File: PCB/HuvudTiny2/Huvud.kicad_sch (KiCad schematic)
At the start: 104 parts, among them J1 Vin, J12 USB_Micro-B, J2 DBG, J3 THERM, J4 FAN0, J5 FAN1, J6 Heater, J7 Endstop, J9 STEPPER, Q1 AO3400A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

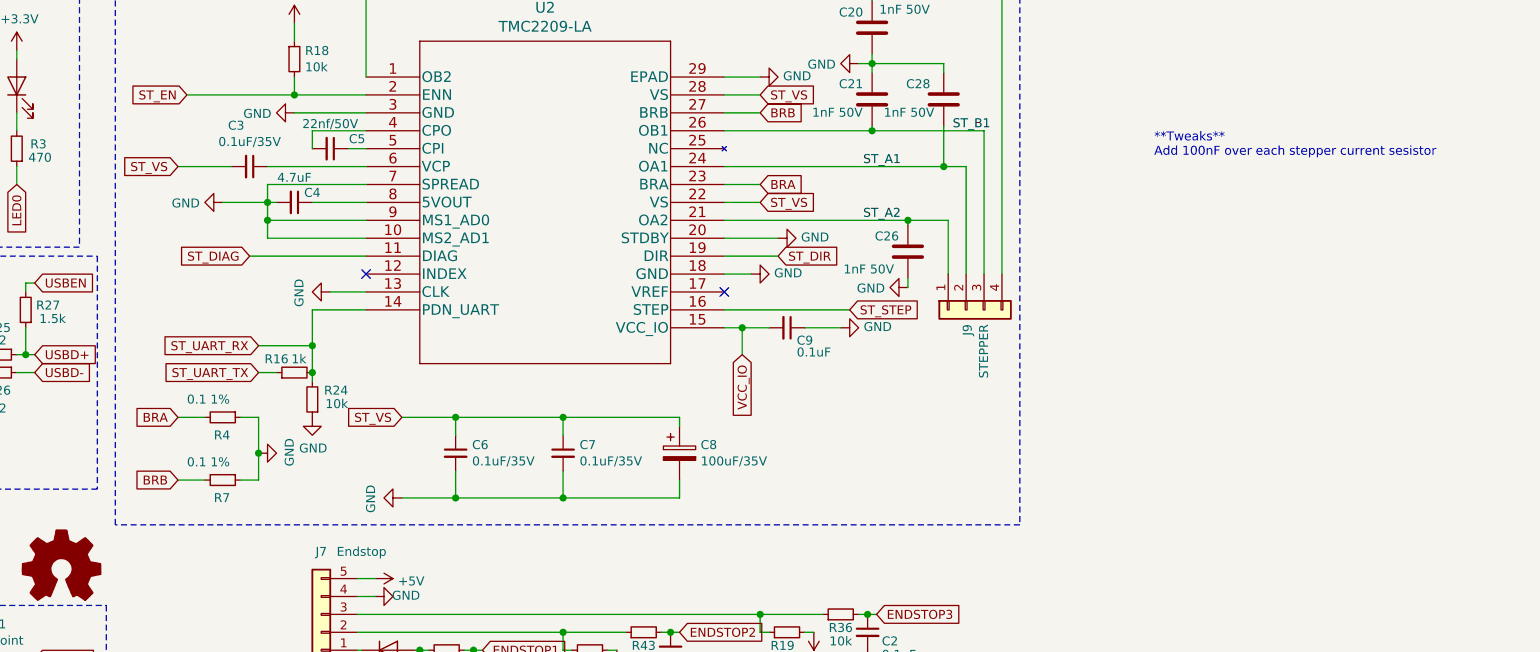
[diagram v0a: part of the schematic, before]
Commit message: Add caps across current sense resistors.
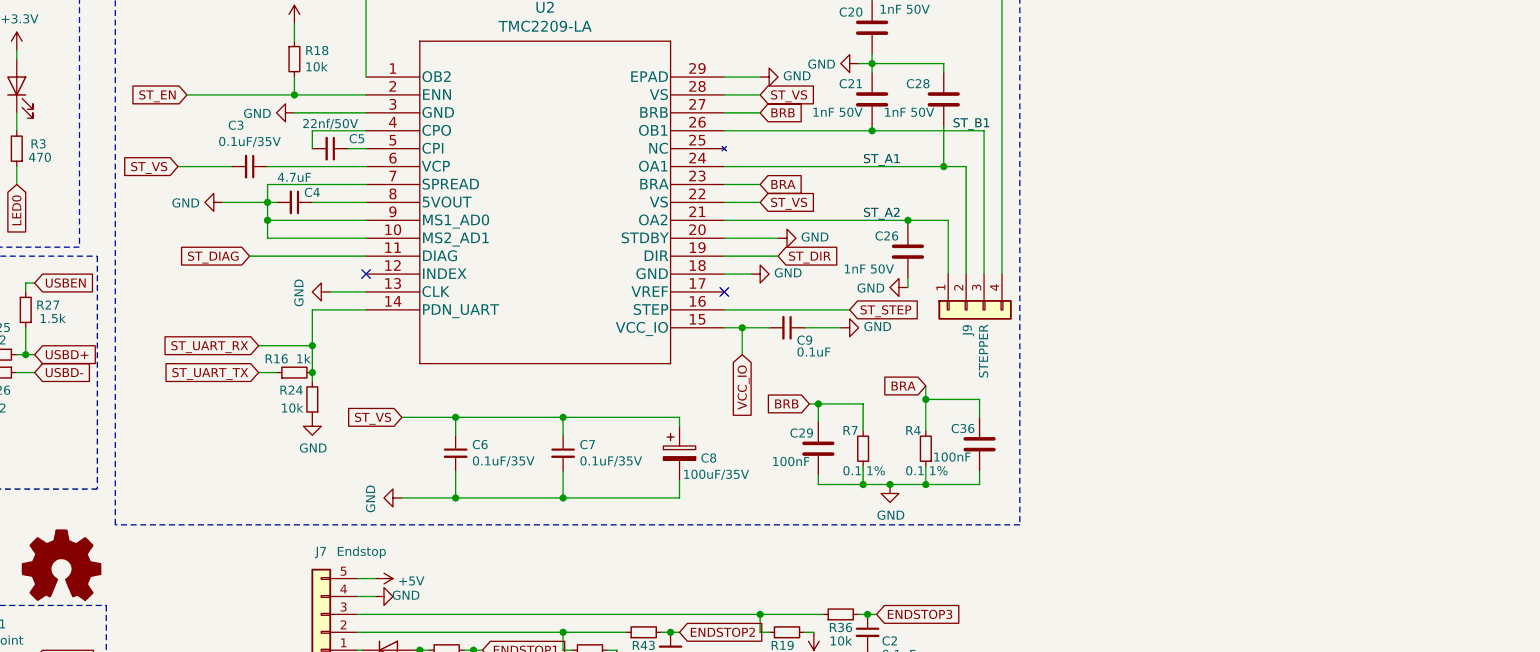
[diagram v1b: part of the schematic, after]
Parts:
- added C29, C36: 100nF, Capacitor_SMD:C_0402_1005Metric, symbol Device:C
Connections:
- net BRA: now also C36.1
- net BRB: now also C29.1
- net GND: now also C29.2, C36.2
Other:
- note removed: "**Tweaks** Add 100nF over each stepper current sesistor"
- moved on the sheet: R4, R7

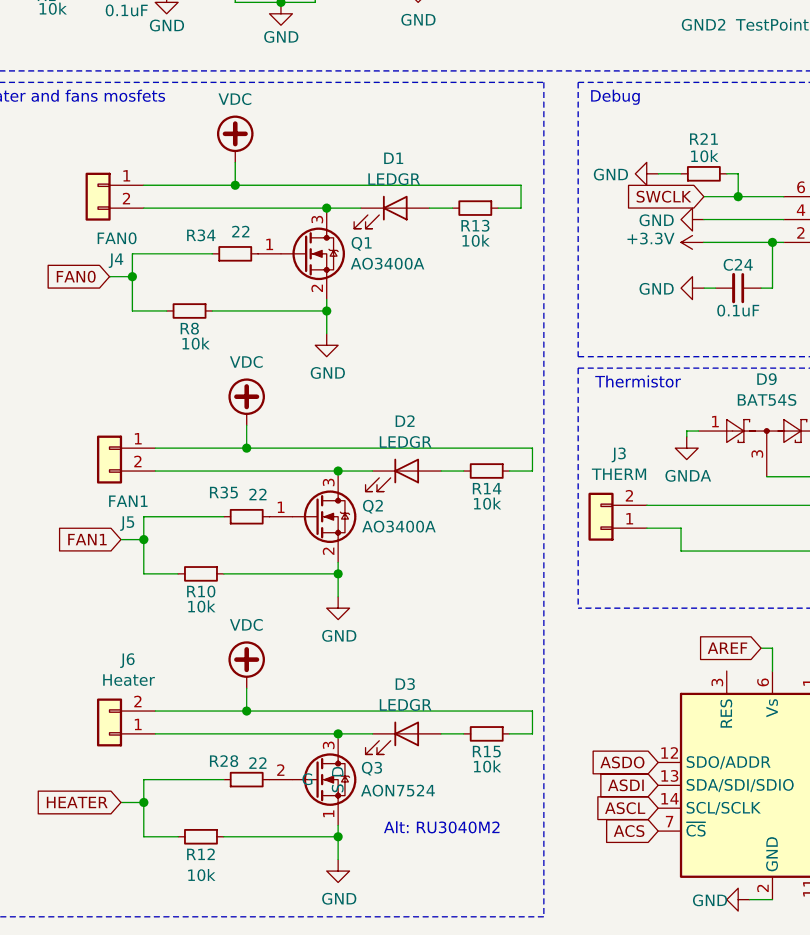
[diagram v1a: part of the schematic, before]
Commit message: Small tweaks to footprints.
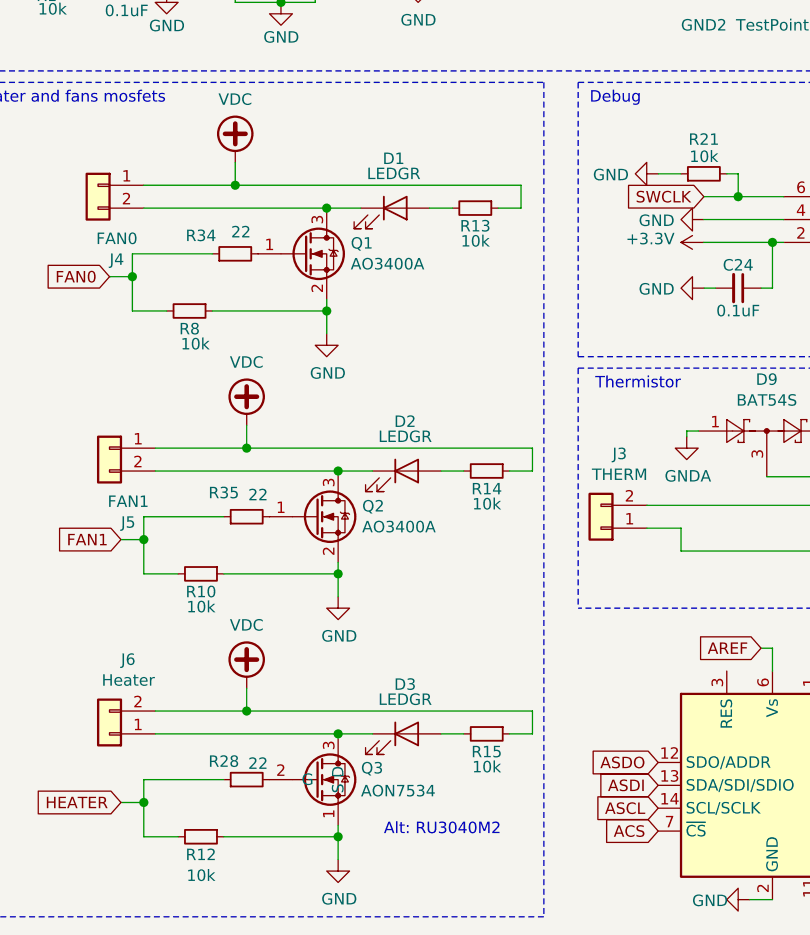
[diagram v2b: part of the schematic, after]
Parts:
- C22: footprint Capacitor_SMD:C_1210_3225Metric -> Capacitor_SMD:C_1206_3216Metric
- Q3: value AON7524 -> AON7534
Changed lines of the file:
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@@
     (property "Reference" "C22" (id 0) (at 251.46 151.765 0))
     (property "Value" "10uF/35V" (id 1) (at 255.905 149.225 90))
-    (property "Footprint" "Capacitor_SMD:C_1210_3225Metric" (id 2) (at 253.365 149.86 0)
+    (property "Footprint" "Capacitor_SMD:C_1206_3216Metric" (id 2) (at 253.365 149.86 0)
       (effects (font (size 1.27 1.27)) hide)
     )
@@
     (in_bom yes) (on_board yes)
     (property "Reference" "D1" (id 0) (at 60.7822 111.3536 0))
-    (property "Value" "LEDGR" (id 1) (at 60.7822 113.665 0))
+    (property "Value" "LEDGR" (id 1) (at 60.7822 113.03 0))
     (property "Footprint" "LED_SMD:LED_0402_1005Metric" (id 2) (at 60.96 116.84 0)
       (effects (font (size 1.27 1.27)) hide)
@@
     (in_bom yes) (on_board yes)
     (property "Reference" "D2" (id 0) (at 62.0522 140.5636 0))
-    (property "Value" "LEDGR" (id 1) (at 62.0522 142.875 0))
+    (property "Value" "LEDGR" (id 1) (at 62.0522 142.24 0))
     (property "Footprint" "LED_SMD:LED_0402_1005Metric" (id 2) (at 62.23 146.05 0)
       (effects (font (size 1.27 1.27)) hide)
@@
     (in_bom yes) (on_board yes)
     (property "Reference" "D3" (id 0) (at 62.0522 169.7736 0))
-    (property "Value" "LEDGR" (id 1) (at 62.0522 172.085 0))
+    (property "Value" "LEDGR" (id 1) (at 62.0522 171.45 0))
     (property "Footprint" "LED_SMD:LED_0402_1005Metric" (id 2) (at 62.23 175.26 0)
       (effects (font (size 1.27 1.27)) hide)
@@
       (effects (font (size 1.27 1.27)) (justify left))
     )
-    (property "Value" "AON7524" (id 1) (at 57.15 181.61 0)
+    (property "Value" "AON7534" (id 1) (at 57.15 181.61 0)
       (effects (font (size 1.27 1.27)) (justify left))
     )
@@
     )
     (path "/00000000-0000-0000-0000-00005f85ea85"
-      (reference "C22") (unit 1) (value "10uF/35V") (footprint "Capacitor_SMD:C_1210_3225Metric")
+      (reference "C22") (unit 1) (value "10uF/35V") (footprint "Capacitor_SMD:C_1206_3216Metric")
     )
     (path "/00000000-0000-0000-0000-00005f59faa3"
@@
     )
     (path "/00000000-0000-0000-0000-00005f1a1e38"
-      (reference "Q3") (unit 1) (value "AON7524") (footprint "Huvud:DFN-8-1EP_3x3mm_P0.65mm_EP1.7x2.05mm")
+      (reference "Q3") (unit 1) (value "AON7534") (footprint "Huvud:DFN-8-1EP_3x3mm_P0.65mm_EP1.7x2.05mm")
     )
     (path "/00000000-0000-0000-0000-00005f443551"

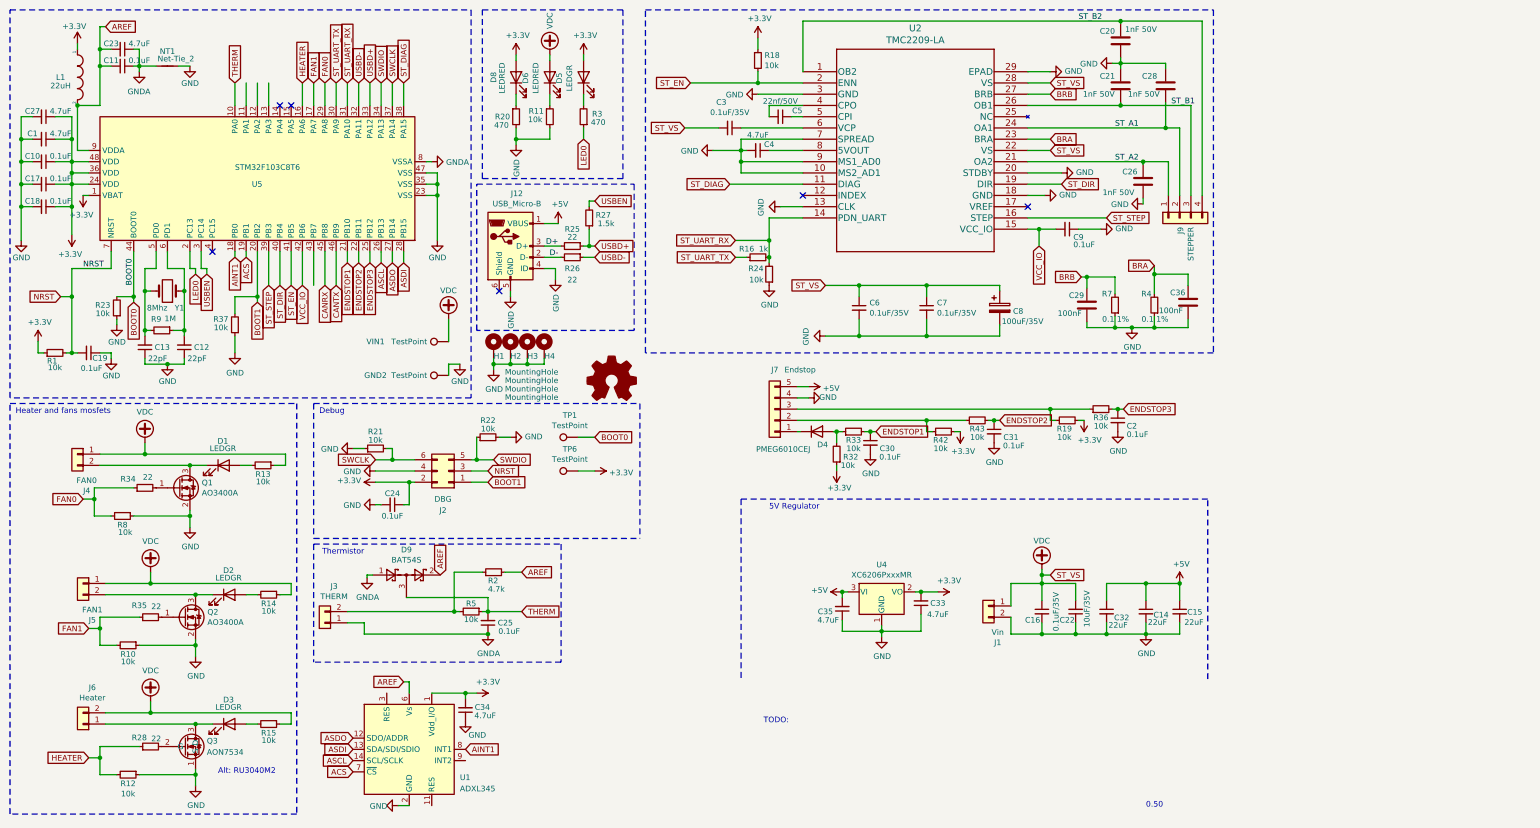
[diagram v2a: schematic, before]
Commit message: Replaced MCU with SAMD21
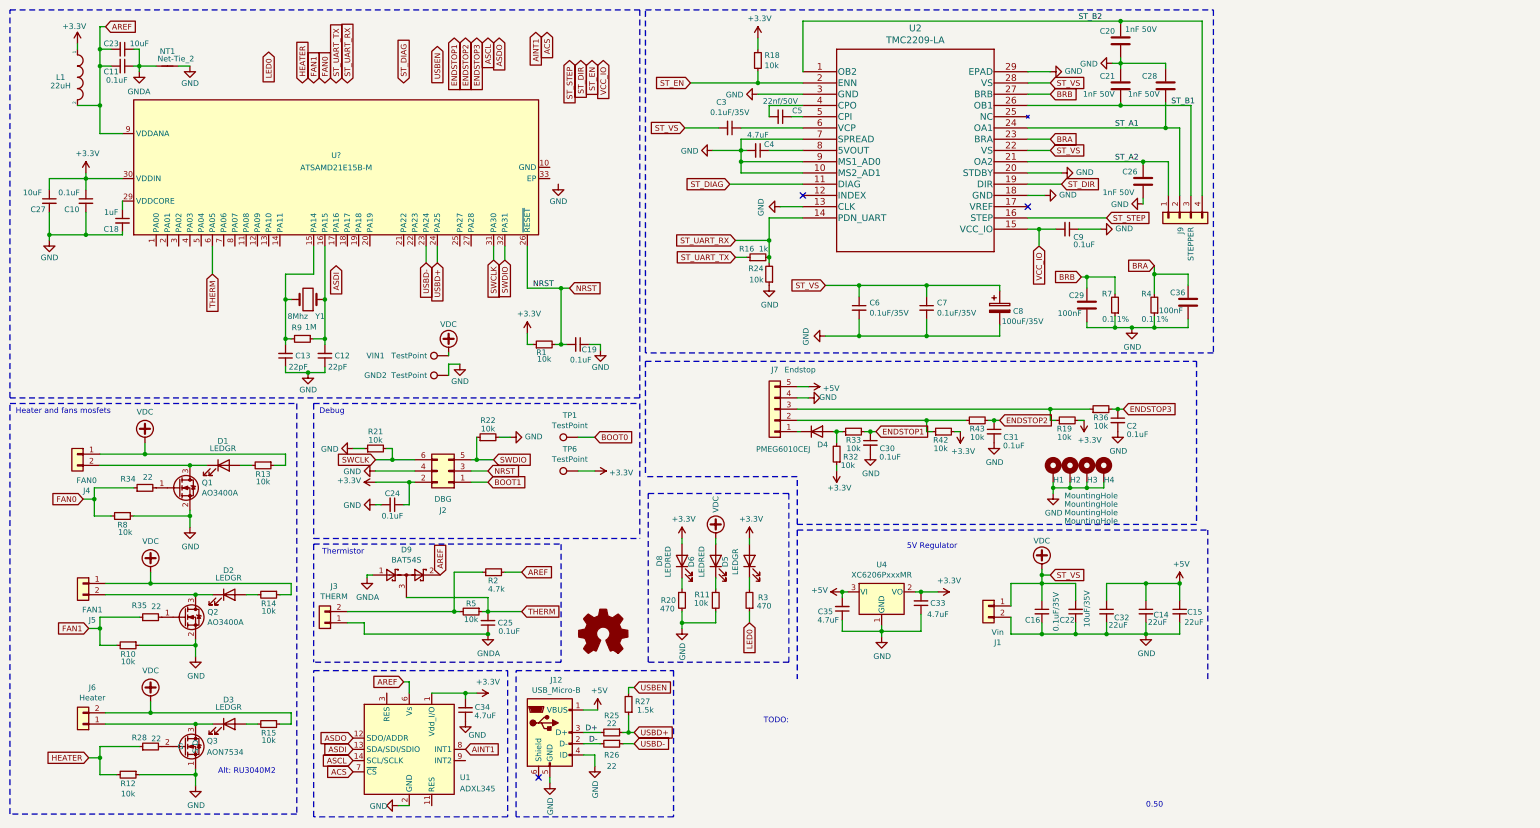
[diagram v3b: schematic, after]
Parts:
- removed C1: 4.7uF, Capacitor_SMD:C_0402_1005Metric, symbol Device:C_Small
- removed C17: 0.1uF, Capacitor_SMD:C_0402_1005Metric, symbol Device:C_Small
- removed R23, R37: 10k, Resistor_SMD:R_0402_1005Metric, symbol Device:R_Small
- removed U5: STM32F103C8T6, Package_QFP:LQFP-48_7x7mm_P0.5mm, symbol MCU_ST_STM32F1:STM32F103C8Tx
- added U?: ATSAMD21E15B-M, Package_DFN_QFN:QFN-32-1EP_5x5mm_P0.5mm_EP3.6x3.6mm, symbol MCU_Microchip_SAMD:ATSAMD21E15B-M
- C18: value 0.1uF -> 1uF; LCSC C1525 -> C52923
- C23, C27: value 4.7uF -> 10uF; LCSC C23733 -> C15525
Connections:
- net +3V3: now also U?.30 (VDDIN); no longer C18.1
- net AREF: now also U?.9 (VDDANA)
- net NRST: now also U?.26 (~{RESET})
- net SWCLK: now also U?.31 (PA30)
- net SWDIO: now also U?.32 (PA31)
- net THERM: now also U?.6 (PA05)
- net USBD+: now also U?.24 (PA25)
- net USBD-: now also U?.23 (PA24)
- net at C13.2, R9.2, Y1.2: now also U?.15 (PA14)
- net at C12.2, R9.1, Y1.1: now also U?.16 (PA15)
- new net: C18.1, U?.29 (VDDCORE)
- new net: U?.10 (GND), U?.28 (GND)
- no-connect marks 6 -> 3
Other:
- moved on the sheet: C10, C12, C13, C18, C19, C27, D5, D6, D8, H1, H2, H3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

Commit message: Some routing.
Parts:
- removed GND2, TP1, TP6, VIN1: TestPoint, TestPoint:TestPoint_Pad_D1.0mm, symbol Connector:TestPoint
- removed R27: 1.5k, Resistor_SMD:R_0402_1005Metric, symbol Device:R_Small
- removed R9: 1M, Resistor_SMD:R_0402_1005Metric, symbol Device:R_Small
- added R6: 1k, Resistor_SMD:R_0402_1005Metric, symbol Device:R_Small
- gave numbers to parts that had none: 1
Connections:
- net +3V3: now also R6.1
- net ACS: now also U3.19 (PA18)
- net AINT1: now also U3.5 (PA04)
- net ASCL: now also U3.18 (PA17)
- net ASDI: now also U3.17 (PA16)
- net ASDO: now also U3.20 (PA19)
- net ENDSTOP1: now also U3.1 (PA00)
- net ENDSTOP2: now also U3.2 (PA01)
- net ENDSTOP3: now also U3.3 (PA02)
- net FAN0: now also U3.8 (PA07)
- net FAN1: now also U3.11 (PA08)
- net GND: now also U3.10 (GND), U3.28 (GND), U3.33 (EP)
- net HEATER: now also U3.7 (PA06)
- net LED0: now also U3.25 (PA27)
- net ST_DIAG: now also U3.4 (PA03)
- net ST_DIR: now also U3.22 (PA23)
- net ST_EN: now also U3.12 (PA09)
- net ST_STEP: now also U3.21 (PA22)
- net ST_UART_RX: now also U3.14 (PA11)
- net ST_UART_TX: now also U3.13 (PA10)
- net SWCLK: now also R6.2
- net VCC_IO: now also U3.27 (PA28)
- net BOOT1: no longer names the net of J2.1 (Pin_1)
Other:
- moved on the sheet: C12, C13, Y1

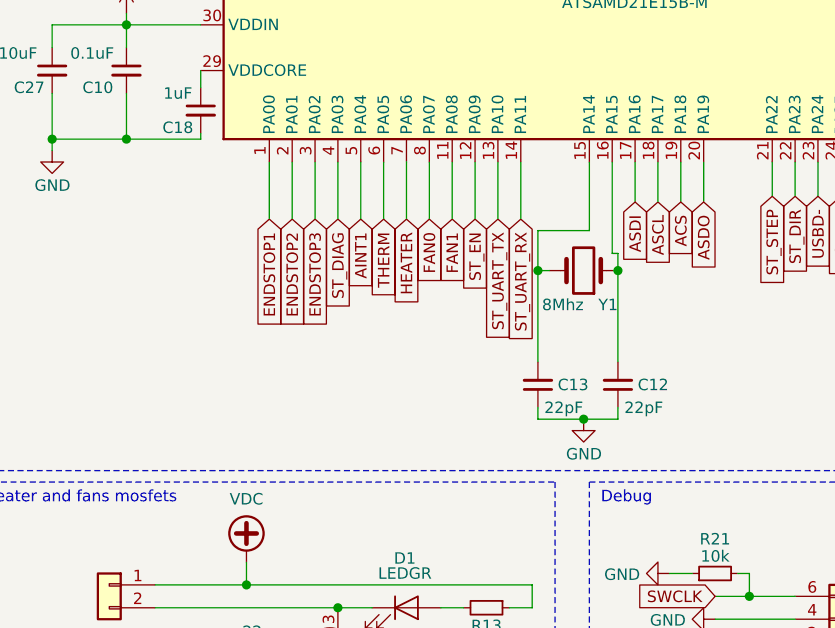
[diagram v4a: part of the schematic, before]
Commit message: Routed with 32k crystal.
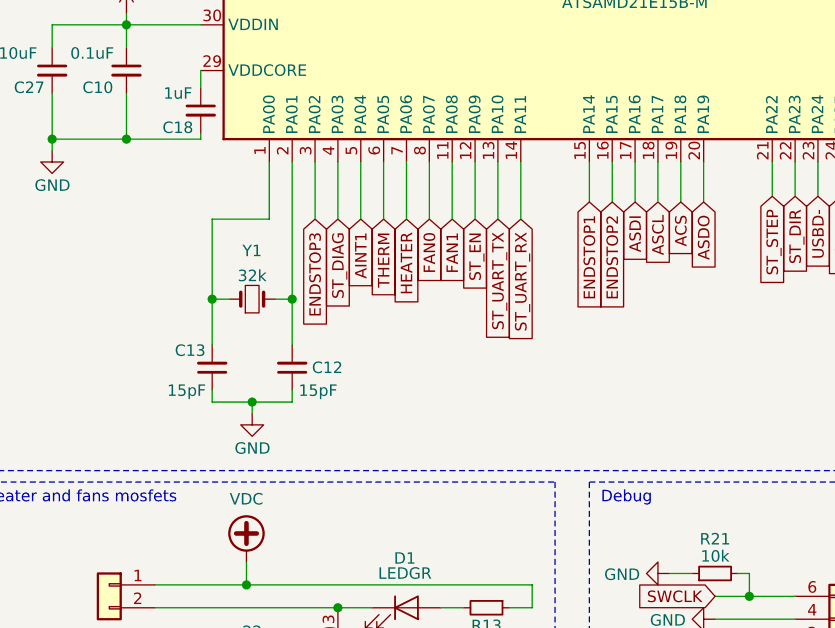
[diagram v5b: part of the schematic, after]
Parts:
- removed Y1: 8Mhz, Crystal:Crystal_SMD_5032-2Pin_5.0x3.2mm, symbol Device:Crystal
- added Y1: 32k, Crystal:Crystal_SMD_3215-2Pin_3.2x1.5mm, symbol Device:Crystal_Small
- C12, C13: value 22pF -> 15pF; LCSC C1555 -> C1548
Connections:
- net ENDSTOP1: now also U3.15 (PA14); no longer U3.1 (PA00)
- net ENDSTOP2: now also U3.16 (PA15); no longer U3.2 (PA01)
- net at C12.2: now also U3.2 (PA01), Y1.2; no longer U3.16 (PA15)
- net at C13.2: now also U3.1 (PA00), Y1.1; no longer U3.15 (PA14)
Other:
- moved on the sheet: C12, C13
